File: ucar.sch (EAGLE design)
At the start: 46 parts, among them IC1 L298, T1 2SC1815, T2 2SC1815

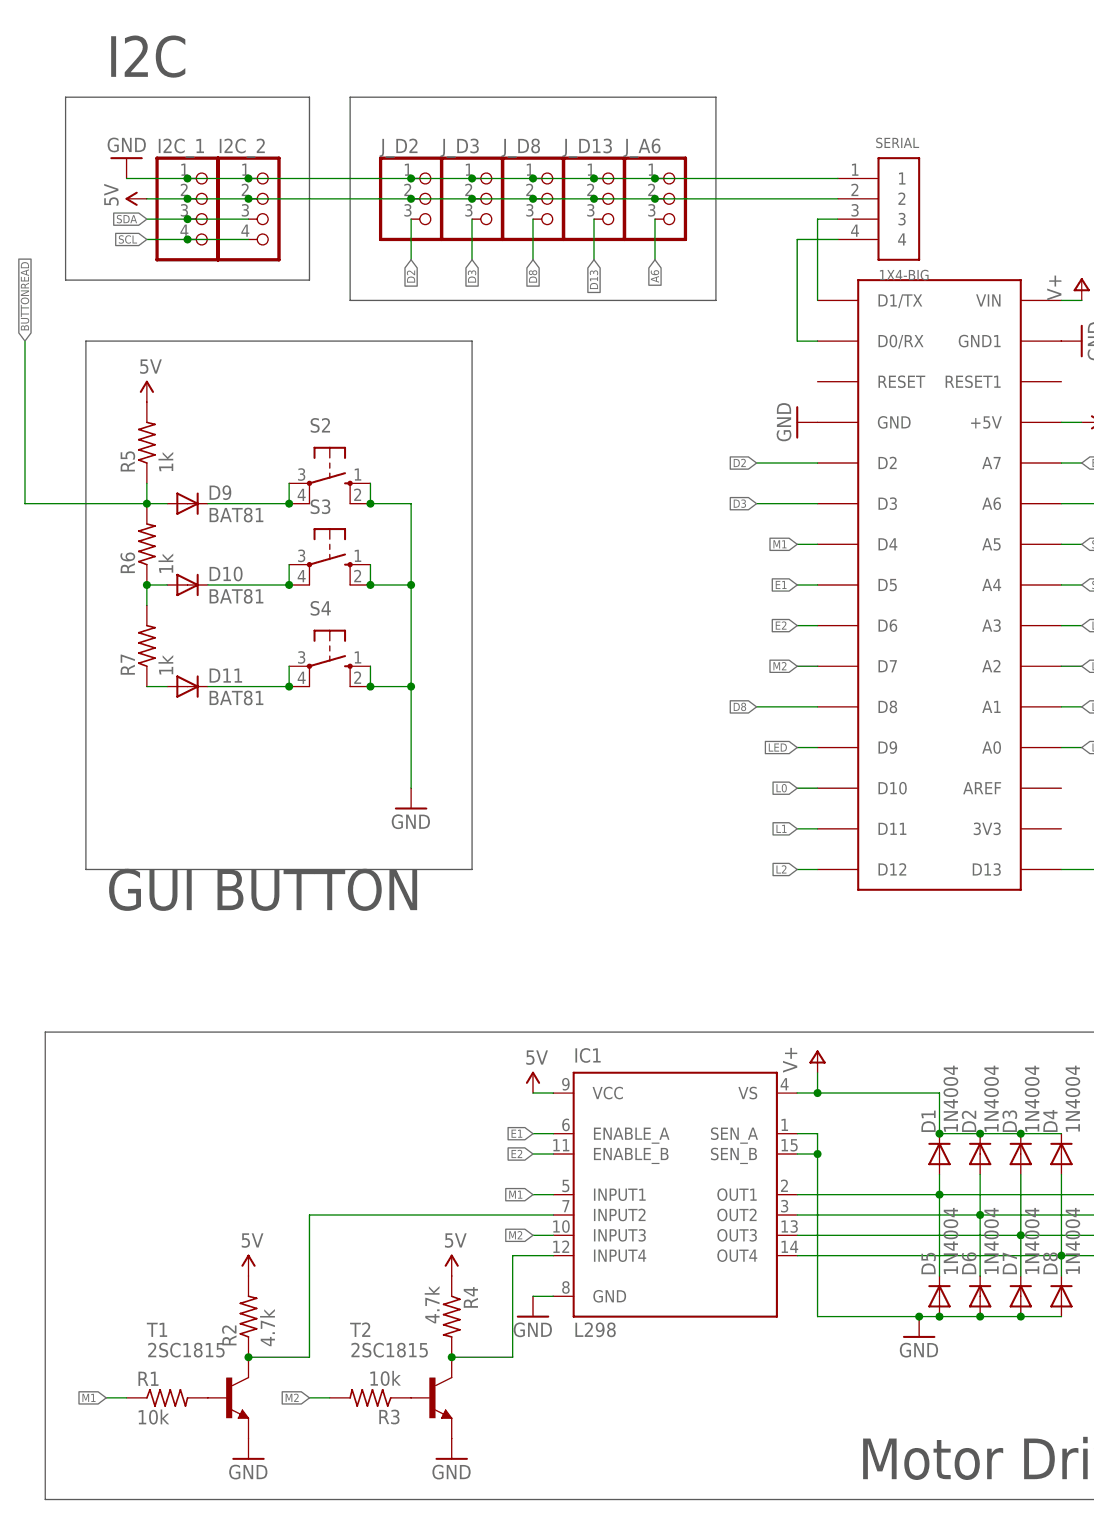
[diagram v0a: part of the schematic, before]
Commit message: tamiya version
using Tamiya 70093 gearbox for the car
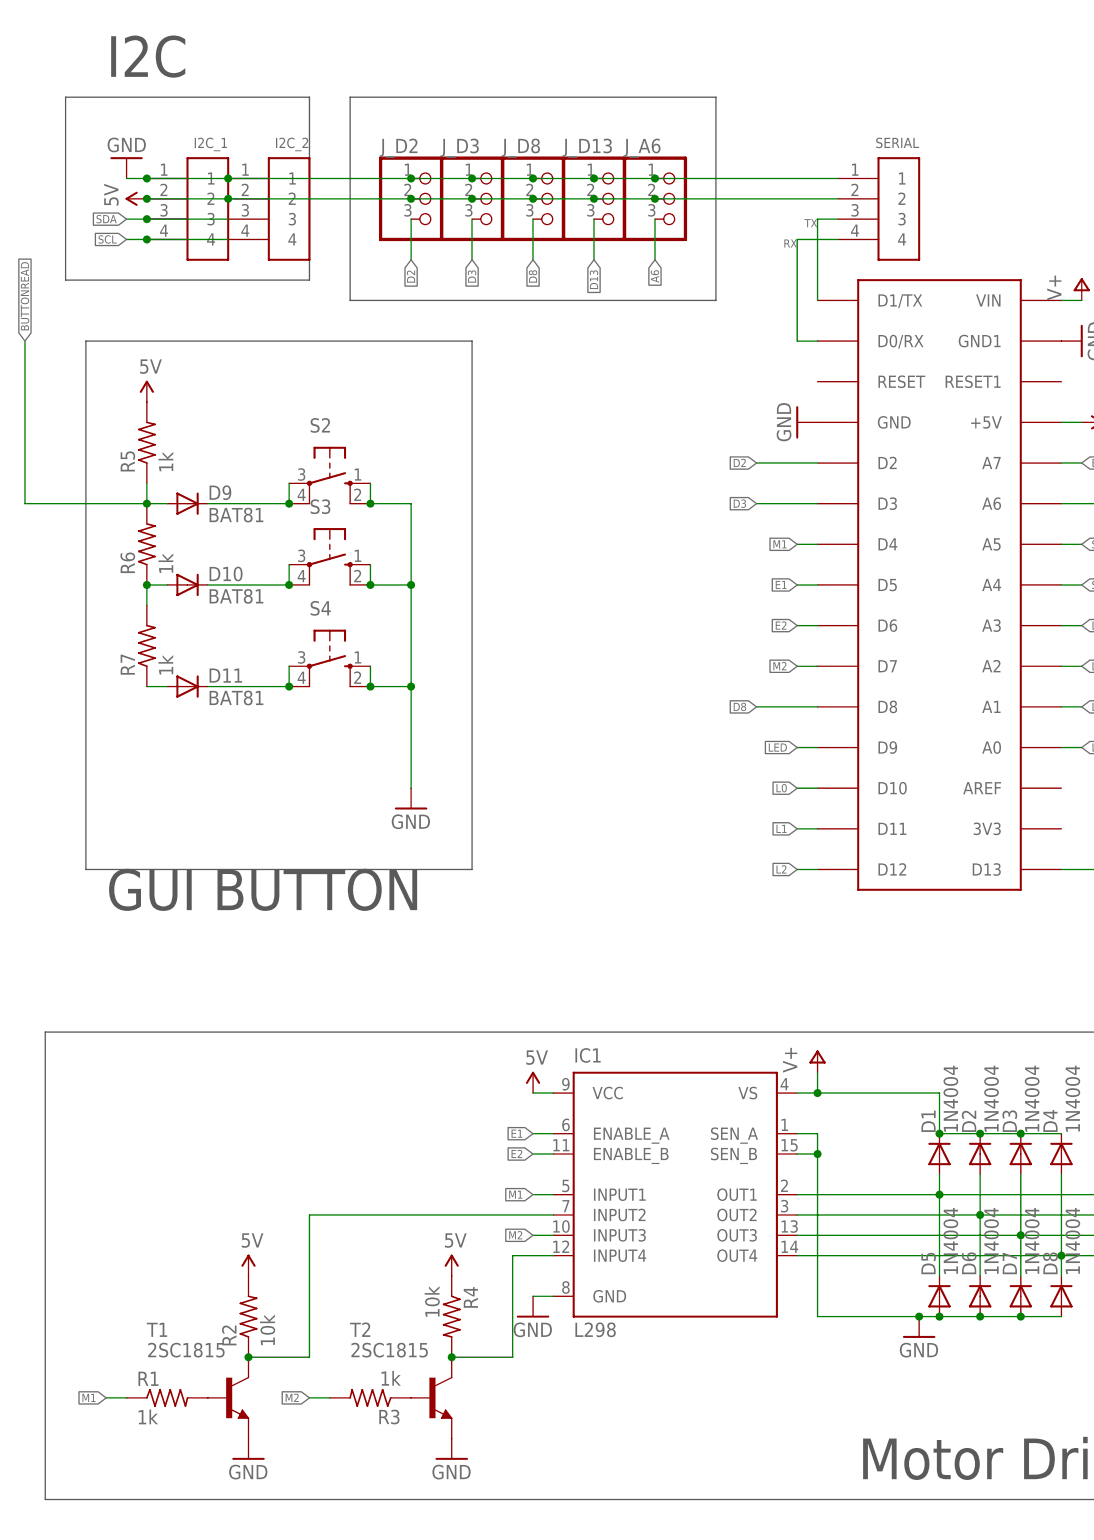
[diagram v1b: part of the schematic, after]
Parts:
- I2C_1, I2C_2: value (none) -> 1X4-BIG; device pinhead:PINHD-1X4 -> adafruit:1X4-BIG
- R1, R3: value 10k -> 1k
- R2, R4: value 4.7k -> 10k
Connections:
- net N$11 renamed TX
- net N$17 renamed RX
